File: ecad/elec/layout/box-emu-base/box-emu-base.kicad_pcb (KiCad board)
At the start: 2 copper layers, 72.5 x 63.9 mm, 54 parts

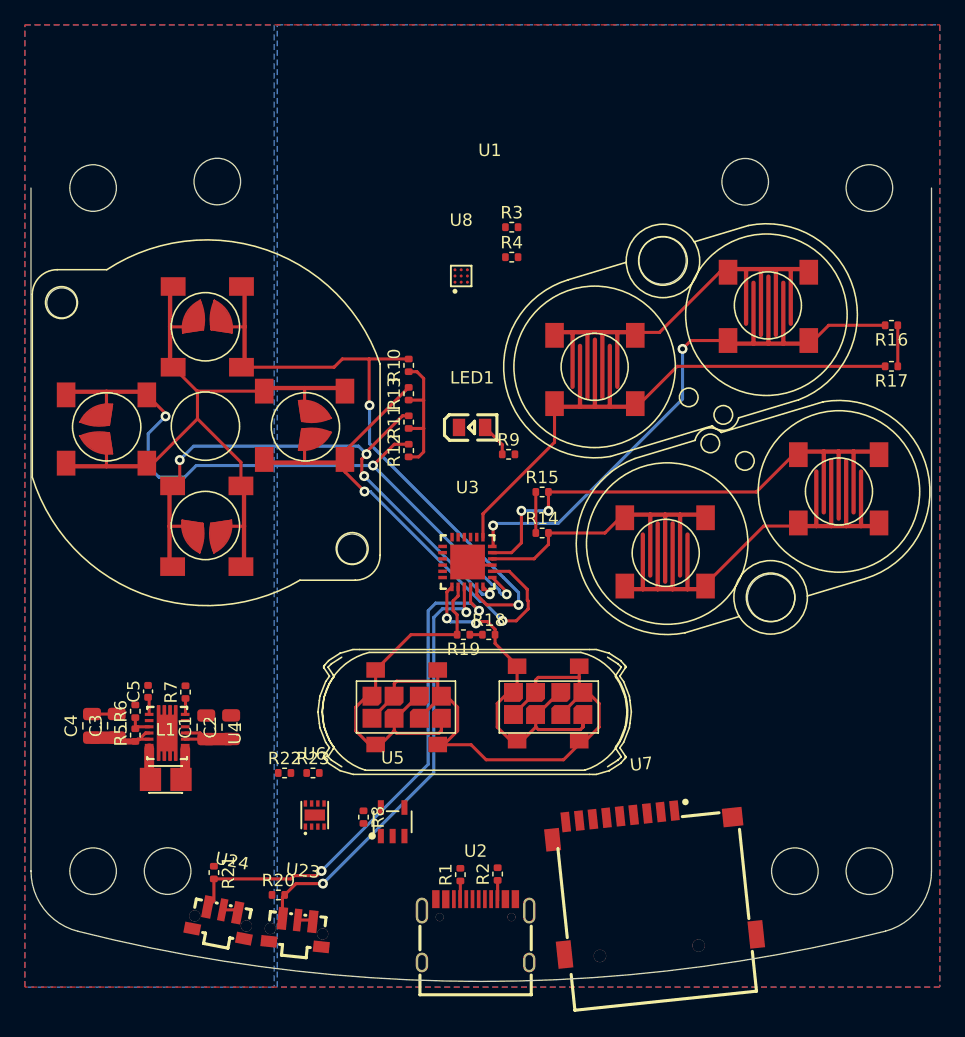
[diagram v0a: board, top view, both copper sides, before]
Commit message: update layouts to use latest footprints and fixed volume buttons and include address pins
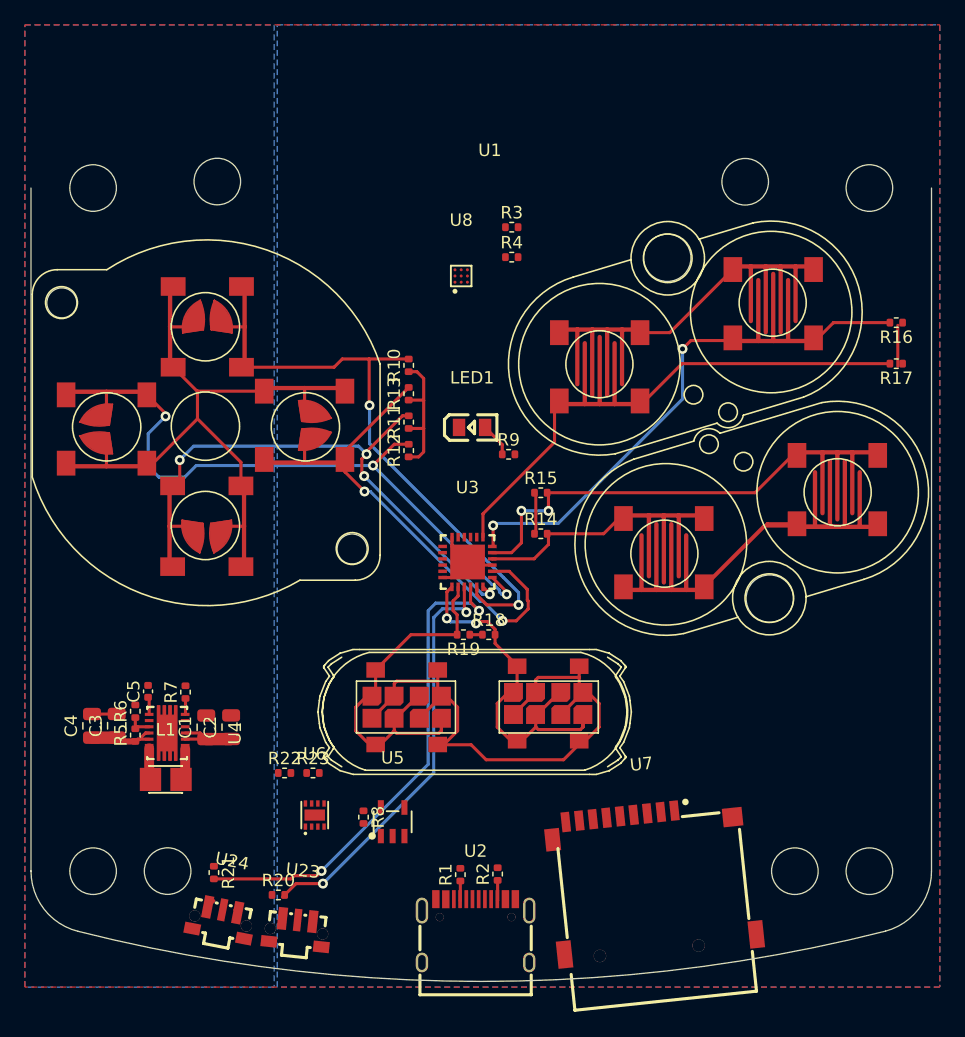
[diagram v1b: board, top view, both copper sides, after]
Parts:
- R6: value 62.5mW Thick Film Resistors 50V ±100ppm/℃ ±0.5% 27.4kΩ 0402 Chip Resistor - Surface Mount ROHS -> 62.5mW Thick Film Resistors 50V ±100ppm/℃ ±1% 27.4kΩ 0402 Chip Resistor - Surface Mount ROHS
- moved U17 0.44 mm to (145.6, 59.4)
- moved U18 0.44 mm to (152.6, 57.0)
- moved U19 0.44 mm to (138.7, 62.0)
- moved R16 0.44 mm to (162.5, 58.5)
- moved R17 0.44 mm to (162.5, 61.8)
- moved R14 0.12 mm to (133.9, 75.5)
- moved R15 0.12 mm to (133.9, 72.2)
- moved U15 0.12 mm to (143.8, 77.0)
- moved U16 0.12 mm to (157.8, 71.9)
- moved U14 0.12 mm to (150.8, 74.6)
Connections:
- U23 pad 1: p1_2 -> vcc
- U23 pad 2: vcc -> p1_2
- U24 pad 1: p1_3 -> vcc
- U24 pad 2: vcc -> p1_3
- U3 pad 18: ad0 -> gnd
- U3 pad 24: ad1 -> gnd
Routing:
- net vcc: track 50.9 -> 68.5 mm
- net (no net): track 12.5 -> 0.00 mm
- net gnd: track 22.8 -> 27.9 mm
- net p1_3: track 42.7 -> 40.3 mm
- net p1_2: track 35.7 -> 34.0 mm
- added copper zone on B.Cu, net (none)
- added copper zone on F.Cu, net (none)
- removed copper zone on B.Cu, net 3V3
- removed copper zone on B.Cu, net 5V
- removed copper zone on F.Cu, net GND

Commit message: updated footprints for the pmod headers and moved step files into .3dshapes folder
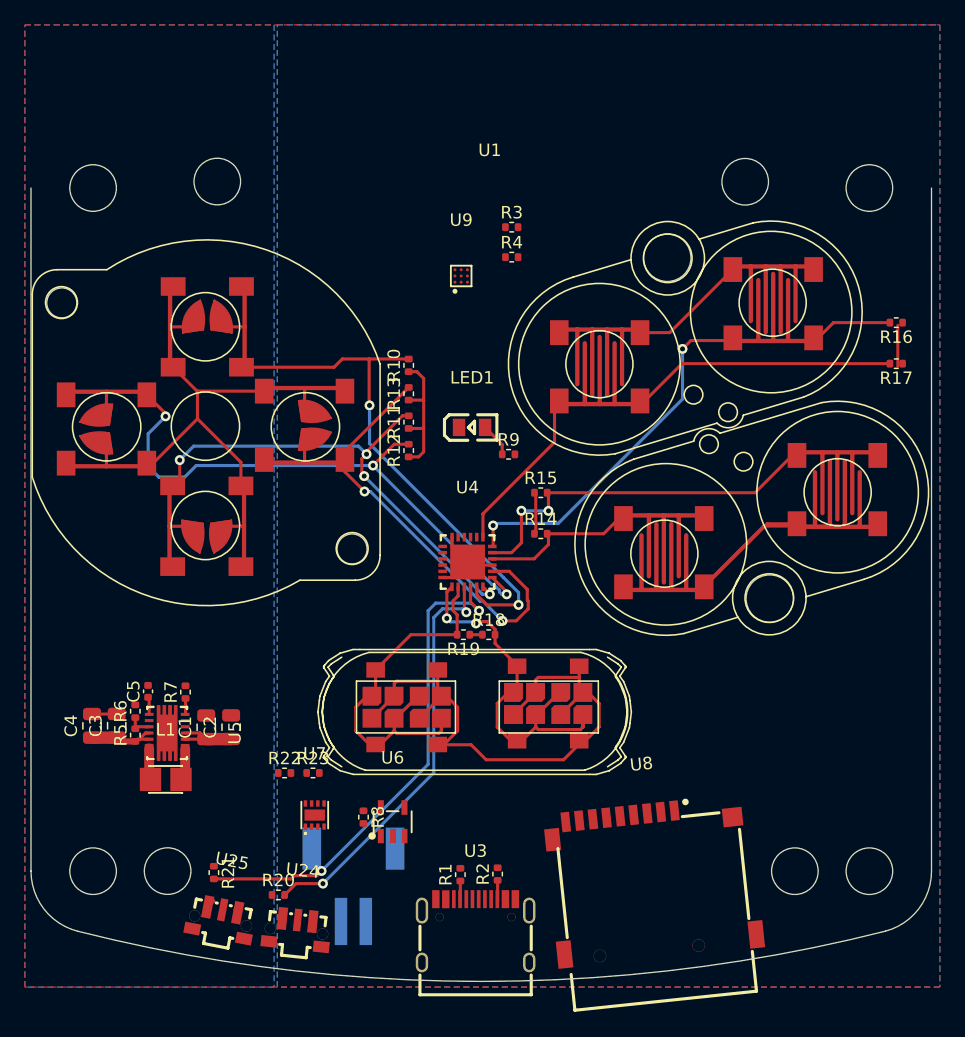
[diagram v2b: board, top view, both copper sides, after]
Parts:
- added U2: , lib:CONN-SMD_P2.00_S2B-PH-SM4-TB-LF-SN, B.Cu at (118.8, 103.8)
- renumbered U9 to U10, U10 to U11, U11 to U12, U12 to U13, U13 to U14, U14 to U15, U15 to U16, U16 to U17, U17 to U18, U18 to U19, U19 to U20, U20 to U21, U21 to U22, U22 to U23, U23 to U24, U24 to U25, U2 to U3, U3 to U4, U4 to U5, U5 to U6, U6 to U7, U7 to U8, U8 to U9
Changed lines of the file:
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@@
     (at 103.828721 91.523474 -90)
     (attr smd)
-    (fp_text reference "U4" (at 0 -5.45 90) (layer "F.SilkS")
+    (fp_text reference "U5" (at 0 -5.45 90) (layer "F.SilkS")
         (effects (font (size 1 1) (thickness 0.15)))
     )
@@
     (at 108.113453 106.722937 -11)
     (attr smd)
-    (fp_text reference "U24" (at 0 -4.98 169) (layer "F.SilkS")
+    (fp_text reference "U25" (at 0 -4.98 169) (layer "F.SilkS")
         (effects (font (size 1 1) (thickness 0.15)))
     )
@@
   (footprint "lib:GAMEBOY_COLOR_START_SELECT_MEMBRANE" (layer "F.Cu")
     (at 128.3352 89.4669)
-    (fp_text reference "U20" (at 0 0) (layer "F.SilkS") hide
+    (fp_text reference "U21" (at 0 0) (layer "F.SilkS") hide
         (effects (font (size 1.27 1.27) (thickness 0.15)))
     )
@@
     (at 121.981 98.672)
     (attr smd)
-    (fp_text reference "U5" (at 0 -5.15) (layer "F.SilkS")
+    (fp_text reference "U6" (at 0 -5.15) (layer "F.SilkS")
         (effects (font (size 1 1) (thickness 0.15)))
     )
@@
   (footprint "lib:GBC_DPAD_BUTTON" (layer "F.Cu")
     (at 107.018 74.879 90)
-    (fp_text reference "U11" (at -1.81 -3.429 90) (layer "F.SilkS") hide
+    (fp_text reference "U12" (at -1.81 -3.429 90) (layer "F.SilkS") hide
         (effects (font (size 0.666496 0.666496) (thickness 0.146304)) (justify left bottom))
     )
@@
     (at 127.5 54.729)
     (attr smd)
-    (fp_text reference "U8" (at 0 -4.5) (layer "F.SilkS")
+    (fp_text reference "U9" (at 0 -4.5) (layer "F.SilkS")
         (effects (font (size 1 1) (thickness 0.15)))
     )
@@
   (footprint "lib:GBC_START_SELECT_BUTTON" (layer "F.Cu")
     (at 134.502 89.147 90)
-    (fp_text reference "U21" (at -6.35 -4.699 90) (layer "F.SilkS") hide
+    (fp_text reference "U22" (at -6.35 -4.699 90) (layer "F.SilkS") hide
         (effects (font (size 0.666496 0.666496) (thickness 0.146304)) (justify left bottom))
     )
@@
   (footprint "lib:GBC_DPAD_BUTTON" (layer "F.Cu")
     (at 114.892 66.751 180)
-    (fp_text reference "U13" (at -1.81 -3.429) (layer "F.SilkS") hide
+    (fp_text reference "U14" (at -1.81 -3.429) (layer "F.SilkS") hide
         (effects (font (size 0.666496 0.666496) (thickness 0.146304)) (justify right bottom))
     )
@@
     (at 142.986109 103.27631 6)
     (attr smd)
-    (fp_text reference "U7" (at 0 -9.3 6) (layer "F.SilkS")
+    (fp_text reference "U8" (at 0 -9.3 6) (layer "F.SilkS")
         (effects (font (size 1 1) (thickness 0.15)))
     )
@@
   (footprint "lib:GBC_A_B_BUTTON" (layer "F.Cu")
     (at 138.650695 62.041068 180)
-    (fp_text reference "U19" (at -1.81 -3.429) (layer "F.SilkS") hide
+    (fp_text reference "U20" (at -1.81 -3.429) (layer "F.SilkS") hide
         (effects (font (size 0.666496 0.666496) (thickness 0.146304)) (justify left top))
     )
@@
     (at 128.6602 107.4486)
     (attr smd)
-    (fp_text reference "U2" (at 0 -6.42) (layer "F.SilkS")
+    (fp_text reference "U3" (at 0 -6.42) (layer "F.SilkS")
         (effects (font (size 1 1) (thickness 0.15)))
     )
@@
     (at 115.709 98.13)
     (attr smd)
-    (fp_text reference "U6" (at 0 -4.93) (layer "F.SilkS")
+    (fp_text reference "U7" (at 0 -4.93) (layer "F.SilkS")
         (effects (font (size 1 1) (thickness 0.15)))
     )
@@
   (footprint "lib:GBC_A_B_BUTTON" (layer "F.Cu")
     (at 152.620695 56.961068 180)
-    (fp_text reference "U18" (at -1.81 -3.429) (layer "F.SilkS") hide
+    (fp_text reference "U19" (at -1.81 -3.429) (layer "F.SilkS") hide
         (effects (font (size 0.666496 0.666496) (thickness 0.146304)) (justify left top))
     )
@@
   (footprint "lib:GAMEBOY_COLOR_A_B_BUTTON_MEMBRANE" (layer "F.Cu")
     (at 145.617445 59.361352 180)
-    (fp_text reference "U17" (at 0 0) (layer "F.SilkS") hide
+    (fp_text reference "U18" (at 0 0) (layer "F.SilkS") hide
         (effects (font (size 1.27 1.27) (thickness 0.15)) (justify left top))
     )
@@
   (footprint "lib:GBC_DPAD_BUTTON" (layer "F.Cu")
     (at 98.942 67.049)
-    (fp_text reference "U12" (at -1.81 -3.429 180) (layer "F.SilkS") hide
+    (fp_text reference "U13" (at -1.81 -3.429 180) (layer "F.SilkS") hide
         (effects (font (size 0.666496 0.666496) (thickness 0.146304)) (justify right bottom))
     )
@@
     (at 114.229858 107.555873 -6)
     (attr smd)
-    (fp_text reference "U23" (at 0 -4.98 174) (layer "F.SilkS")
+    (fp_text reference "U24" (at 0 -4.98 174) (layer "F.SilkS")
         (effects (font (size 1 1) (thickness 0.15)))
     )
@@
   (footprint "lib:GBC_A_B_BUTTON" (layer "F.Cu")
     (at 143.816 77.006)
-    (fp_text reference "U15" (at -1.81 -3.429) (layer "F.SilkS") hide
+    (fp_text reference "U16" (at -1.81 -3.429) (layer "F.SilkS") hide
         (effects (font (size 0.666496 0.666496) (thickness 0.146304)) (justify right top))
     )
@@
   (footprint "lib:GBC_START_SELECT_BUTTON" (layer "F.Cu")
     (at 123.112 89.449 90)
-    (fp_text reference "U22" (at -6.35 -4.699 90) (layer "F.SilkS") hide
+    (fp_text reference "U23" (at -6.35 -4.699 90) (layer "F.SilkS") hide
         (effects (font (size 0.666496 0.666496) (thickness 0.146304)) (justify left bottom))
     )
@@
   (footprint "lib:GBC_DPAD_BUTTON" (layer "F.Cu")
     (at 107.062 58.825 -90)
-    (fp_text reference "U10" (at -1.81 -3.429 90) (layer "F.SilkS") hide
+    (fp_text reference "U11" (at -1.81 -3.429 90) (layer "F.SilkS") hide
         (effects (font (size 0.666496 0.666496) (thickness 0.146304)) (justify right bottom))
     )
@@
   (footprint "lib:GBC_A_B_BUTTON" (layer "F.Cu")
     (at 157.786 71.926)
-    (fp_text reference "U16" (at -1.81 -3.429) (layer "F.SilkS") hide
+    (fp_text reference "U17" (at -1.81 -3.429) (layer "F.SilkS") hide
         (effects (font (size 0.666496 0.666496) (thickness 0.146304)) (justify right top))
     )
@@
     (at 128.004 77.756)
     (attr smd)
-    (fp_text reference "U3" (at 0 -6) (layer "F.SilkS")
+    (fp_text reference "U4" (at 0 -6) (layer "F.SilkS")
         (effects (font (size 1 1) (thickness 0.15)))
     )
@@
   (footprint "lib:GAMEBOY_COLOR_A_B_BUTTON_MEMBRANE" (layer "F.Cu")
     (at 150.81925 74.605716)
-    (fp_text reference "U14" (at 0 0) (layer "F.SilkS") hide
+    (fp_text reference "U15" (at 0 0) (layer "F.SilkS") hide
         (effects (font (size 1.27 1.27) (thickness 0.15)) (justify right top))
     )
@@
   (footprint "lib:GAMEBOY_COLOR_DPAD_MEMBRANE" (layer "F.Cu")
     (at 106.903651 66.725871)
-    (fp_text reference "U9" (at 0 0) (layer "F.SilkS") hide
+    (fp_text reference "U10" (at 0 0) (layer "F.SilkS") hide
         (effects (font (size 1.27 1.27) (thickness 0.15)))
     )
@@
       (scale (xyz 1 1 1))
       (rotate (xyz 0 0 0))
+    )
+  )
+  (footprint "lib:CONN-SMD_P2.00_S2B-PH-SM4-TB-LF-SN" (layer "B.Cu")
+    (at 118.824 103.768)
+    (attr smd)
+    (fp_text reference "U2" (at 0 6.93) (layer "B.SilkS")
+        (effects (font (size 1 1) (thickness 0.15)) (justify mirror))
+    )
+    (fp_text value "" (at 0 -6.93) (layer "B.Fab")
+        (effects (font (size 1 1) (thickness 0.15)) (justify mirror))
+    )
+    (fp_text user "${REFERENCE}" (at 0 0) (layer "B.Fab")
+        (effects (font (size 1 1) (thickness 0.15)) (justify mirror))
+    )
+    (fp_line (start -3.95 3.22) (end -3.95 -1)
+      (stroke (width 0.25) (type solid)) (layer "B.SilkS"))
+    (fp_line (start -3 1.64) (end -3 3.22)
+      (stroke (width 0.25) (type solid)) (layer "B.SilkS"))
+    (fp_line (start -3 3.22) (end -3.95 3.22)
+      (stroke (width 0.25) (type solid)) (layer "B.SilkS"))
+    (fp_line (start -1.73 1.64) (end -3 1.64)
+      (stroke (width 0.25) (type solid)) (layer "B.SilkS"))
+    (fp_line (start 0.27 1.65) (end -0.27 1.65)
+      (stroke (width 0.25) (type solid)) (layer "B.SilkS"))
+    (fp_line (start 2.4 -4.38) (end -2.4 -4.38)
+      (stroke (width 0.25) (type solid)) (layer "B.SilkS"))
+    (fp_line (start 3 1.65) (end 1.73 1.65)
+      (stroke (width 0.25) (type solid)) (layer "B.SilkS"))
+    (fp_line (start 3 3.22) (end 3 1.65)
+      (stroke (width 0.25) (type solid)) (layer "B.SilkS"))
+    (fp_line (start 3.95 3.22) (end 3 3.22)
+      (stroke (width 0.25) (type solid)) (layer "B.SilkS"))
+    (fp_line (start 3.95 3.22) (end 3.95 -1)
+      (stroke (width 0.25) (type solid)) (layer "B.SilkS"))
+    (fp_circle (center -3.95 4.23) (end -3.92 4.23)
+      (stroke (width 0.06) (type solid)) (fill none) (layer "B.Fab"))
+    (pad "1" smd rect (at -1 2.93) (size 1 3.8) (layers "B.Cu" "B.Paste" "B.Mask")
+      (net 5 "vcc-2") (pintype "stereo"))
+    (pad "2" smd rect (at 1 2.93) (size 1 3.8) (layers "B.Cu" "B.Paste" "B.Mask")
+      (net 2 "gnd") (pintype "stereo"))
+    (pad "3" smd rect (at 3.35 -2.93) (size 1.5 3.4) (layers "B.Cu" "B.Paste" "B.Mask")
+      (net 2 "gnd") (pintype "stereo"))
+    (pad "4" smd rect (at -3.35 -2.93) (size 1.5 3.4) (layers "B.Cu" "B.Paste" "B.Mask")
+      (net 2 "gnd") (pintype "stereo"))
+    (model "/Users/bob/esp-cpp/esp-box-emu/ecad/build/footprints/footprints.3dshapes/CONN-SMD_P2.00_S2B-PH-SM4-TB-LF-SN.step"
+      (offset (xyz 0 -0.1 -0))
+      (scale (xyz 1 1 1))
+      (rotate (xyz 0 0 0))

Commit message: WIP fleshing out more of the design
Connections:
- U9 pad A1: (no net) -> en
- U9 pad A2: (no net) -> reg
- U9 pad A3: (no net) -> out_p
- U9 pad B1: (no net) -> in_trig
- U9 pad B2: (no net) -> sda
- U9 pad B3: (no net) -> gnd
- U9 pad C1: (no net) -> scl
- U9 pad C2: (no net) -> vcc
- U9 pad C3: (no net) -> out_m
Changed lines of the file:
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@@
   (net 52 "qstrt")
   (net 53 "max17048-ep")
+  (net 54 "en")
+  (net 55 "reg")
+  (net 56 "out_p")
+  (net 57 "in_trig")
+  (net 58 "out_m")
   (footprint "lib:R0402" (layer "F.Cu")
     (at 123.274 68.785 90)
@@
     (fp_arc (start 8.803709 -4.431131) (mid 12.571848 0.197676) (end 9.101408 5.05368)
       (stroke (width 0.127) (type solid)) (layer "F.SilkS"))
-    (model "/Users/bob/esp-cpp/esp-box-emu/ecad/elec/footprints/STEPS/GBC_START_SELECT_MEMBRANE.step"
-      (offset (xyz 1.9 41.15 0))
+    (model "/Users/bob/esp-cpp/esp-box-emu/ecad/elec/footprints/footprints.3dshapes/GBC_START_SELECT_MEMBRANE.step"
+      (offset (xyz 1.9 41.2 0))
       (scale (xyz 1 1 1))
       (rotate (xyz -90 0 0))
@@
       (net 40 "prog") (pintype "stereo"))
     (model "/Users/bob/esp-cpp/esp-box-emu/ecad/elec/footprints/footprints.3dshapes/SOT-23-5_L2.9-W1.6-H1.1-LS2.8-P0.95.wrl"
-      (offset (xyz -5.41 1.47 -0))
+      (offset (xyz 0 0 0))
       (scale (xyz 1 1 1))
-      (rotate (xyz 0 0 270))
+      (rotate (xyz 0 0 -90))
     )
   )
@@
     (fp_circle (center 0.5 0.5) (end 0.57 0.5)
       (stroke (width 0.15) (type solid)) (fill none) (layer "F.Fab"))
-    (pad "A1" smd circle (at -0.5 0.5) (size 0.24 0.24) (layers "F.Cu" "F.Paste" "F.Mask"))
-    (pad "A2" smd circle (at -0.5 0) (size 0.24 0.24) (layers "F.Cu" "F.Paste" "F.Mask"))
-    (pad "A3" smd circle (at -0.5 -0.5) (size 0.24 0.24) (layers "F.Cu" "F.Paste" "F.Mask"))
-    (pad "B1" smd circle (at 0 0.5) (size 0.24 0.24) (layers "F.Cu" "F.Paste" "F.Mask"))
-    (pad "B2" smd circle (at 0 0) (size 0.24 0.24) (layers "F.Cu" "F.Paste" "F.Mask"))
-    (pad "B3" smd circle (at 0 -0.5) (size 0.24 0.24) (layers "F.Cu" "F.Paste" "F.Mask"))
-    (pad "C1" smd circle (at 0.5 0.5) (size 0.24 0.24) (layers "F.Cu" "F.Paste" "F.Mask"))
-    (pad "C2" smd circle (at 0.5 0) (size 0.24 0.24) (layers "F.Cu" "F.Paste" "F.Mask"))
-    (pad "C3" smd circle (at 0.5 -0.5) (size 0.24 0.24) (layers "F.Cu" "F.Paste" "F.Mask"))
+    (pad "A1" smd circle (at -0.5 0.5) (size 0.24 0.24) (layers "F.Cu" "F.Paste" "F.Mask")
+      (net 54 "en") (pintype "stereo"))
+    (pad "A2" smd circle (at -0.5 0) (size 0.24 0.24) (layers "F.Cu" "F.Paste" "F.Mask")
+      (net 55 "reg") (pintype "stereo"))
+    (pad "A3" smd circle (at -0.5 -0.5) (size 0.24 0.24) (layers "F.Cu" "F.Paste" "F.Mask")
+      (net 56 "out_p") (pintype "stereo"))
+    (pad "B1" smd circle (at 0 0.5) (size 0.24 0.24) (layers "F.Cu" "F.Paste" "F.Mask")
+      (net 57 "in_trig") (pintype "stereo"))
+    (pad "B2" smd circle (at 0 0) (size 0.24 0.24) (layers "F.Cu" "F.Paste" "F.Mask")
+      (net 26 "sda") (pintype "stereo"))
+    (pad "B3" smd circle (at 0 -0.5) (size 0.24 0.24) (layers "F.Cu" "F.Paste" "F.Mask")
+      (net 2 "gnd") (pintype "stereo"))
+    (pad "C1" smd circle (at 0.5 0.5) (size 0.24 0.24) (layers "F.Cu" "F.Paste" "F.Mask")
+      (net 25 "scl") (pintype "stereo"))
+    (pad "C2" smd circle (at 0.5 0) (size 0.24 0.24) (layers "F.Cu" "F.Paste" "F.Mask")
+      (net 27 "vcc") (pintype "stereo"))
+    (pad "C3" smd circle (at 0.5 -0.5) (size 0.24 0.24) (layers "F.Cu" "F.Paste" "F.Mask")
+      (net 58 "out_m") (pintype "stereo"))
     (model "/Users/bob/esp-cpp/esp-box-emu/ecad/elec/footprints/footprints.3dshapes/DSBGA-9_L1.5-W1.5-H0.6-R3-C3-P0.50-BL.wrl"
-      (offset (xyz 1 -0.98 -0))
+      (offset (xyz 0 0 0))
       (scale (xyz 1 1 1))
       (rotate (xyz 0 0 0))
@@
       (stroke (width 0.127) (type solid)) (fill none) (layer "F.SilkS"))
     (pad "" np_thru_hole circle (at 1.524 6.096 180) (size 3.81 3.81) (drill 3.81) (layers "*.Cu" "*.Mask"))
-    (model "/Users/bob/esp-cpp/esp-box-emu/ecad/elec/footprints/STEPS/GBC_A_B_MEMBRANE.step"
-      (offset (xyz -19 20.35 0))
+    (model "/Users/bob/esp-cpp/esp-box-emu/ecad/elec/footprints/footprints.3dshapes/GBC_A_B_MEMBRANE.step"
+      (offset (xyz -19 20.3 0))
       (scale (xyz 1 1 1))
       (rotate (xyz -90 0 0))
@@
       (stroke (width 0.127) (type solid)) (fill none) (layer "F.SilkS"))
     (pad "" np_thru_hole circle (at 1.524 6.096) (size 3.81 3.81) (drill 3.81) (layers "*.Cu" "*.Mask"))
-    (model "/Users/bob/esp-cpp/esp-box-emu/ecad/elec/footprints/STEPS/GBC_A_B_MEMBRANE.step"
-      (offset (xyz -19 20.35 0))
+    (model "/Users/bob/esp-cpp/esp-box-emu/ecad/elec/footprints/footprints.3dshapes/GBC_A_B_MEMBRANE.step"
+      (offset (xyz -19 20.3 0))
       (scale (xyz 1 1 1))
       (rotate (xyz -90 0 0))
@@
     (pad "" np_thru_hole circle (at -11.557 -9.8298) (size 2.413 2.413) (drill 2.413) (layers "*.Cu" "*.Mask"))
     (pad "" np_thru_hole circle (at 11.811 9.9822) (size 2.413 2.413) (drill 2.413) (layers "*.Cu" "*.Mask"))
-    (model "/Users/bob/esp-cpp/esp-box-emu/ecad/elec/footprints/STEPS/GBC_DPAD_MEMBRANE.step"
-      (offset (xyz 24 20.35 0))
+    (model "/Users/bob/esp-cpp/esp-box-emu/ecad/elec/footprints/footprints.3dshapes/GBC_DPAD_MEMBRANE.step"
+      (offset (xyz 24 20.24 0))
       (scale (xyz 1 1 1))
       (rotate (xyz -90 0 0))
